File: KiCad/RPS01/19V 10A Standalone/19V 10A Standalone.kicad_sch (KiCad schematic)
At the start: 33 parts, among them U2 LTC3780EUH-TRPBF

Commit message: 19V 10A Standalone PCB
Updated the standalone 19V 10A PCB. Just needs the connectors.
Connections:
- net BOOST2: no longer Cb(SW2)1.1, D1(2)_19V1.1, L1_19V1.1, QA(1)_19V_2.1, QA(1)_19V_2.2, QA(1)_19V_2.3, QB(2)_19V_1.5, QB(2)_19V_1.6, QB(2)_19V_1.7, QB(2)_19V_1.8, U2.17 (SW2)
- new net SW2: Cb(SW2)1.1, D1(2)_19V1.1, L1_19V1.1, QA(1)_19V_2.1, QA(1)_19V_2.2, QA(1)_19V_2.3, QB(2)_19V_1.5, QB(2)_19V_1.6, QB(2)_19V_1.7, QB(2)_19V_1.8, U2.17 (SW2)
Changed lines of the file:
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@@
 (kicad_sch (version 20230121) (generator eeschema)
   (paper "A4")
-  (junction (at 209.806 79.375) (diameter 0) (color 0 0 0 0)
-  )
   (junction (at 53.34 92.075) (diameter 0) (color 0 0 0 0)
   )
@@
   )
   (junction (at 58.42 99.695) (diameter 0) (color 0 0 0 0)
-  )
-  (junction (at 209.806 132.08) (diameter 0) (color 0 0 0 0)
   )
   (junction (at 231.14 31.115) (diameter 0) (color 0 0 0 0)
@@
     (stroke (width 0) (type default))
   )
+  (wire (pts (xy 217.17 79.375) (xy 217.17 163.83))
+    (stroke (width 0) (type default))
+  )
   (wire (pts (xy 175.8696 114.2746) (xy 185.42 114.3))
     (stroke (width 0) (type default))
@@
     (stroke (width 0) (type default))
   )
+  (wire (pts (xy 184.15 154.94) (xy 184.15 163.83))
+    (stroke (width 0) (type default))
+  )
   (wire (pts (xy 184.15 154.94) (xy 184.15 153.035))
     (stroke (width 0) (type default))
@@
     (stroke (width 0) (type default))
   )
-  (wire (pts (xy 234.6942 138.4026) (xy 234.6942 163.1421))
-    (stroke (width 0) (type default))
-  )
   (wire (pts (xy 53.34 88.773) (xy 53.34 92.075))
     (stroke (width 0) (type default))
@@
     (stroke (width 0) (type default))
   )
-  (wire (pts (xy 209.806 132.08) (xy 213.36 132.08))
-    (stroke (width 0) (type default))
-  )
   (wire (pts (xy 48.26 132.715) (xy 53.975 132.715))
     (stroke (width 0) (type default))
@@
     (stroke (width 0) (type default))
   )
-  (wire (pts (xy 184.15 163.1421) (xy 184.15 154.94))
-    (stroke (width 0) (type default))
-  )
   (wire (pts (xy 233.68 56.515) (xy 233.68 33.655))
     (stroke (width 0) (type default))
@@
     (stroke (width 0) (type default))
   )
-  (wire (pts (xy 184.15 163.1421) (xy 234.6942 163.1421))
-    (stroke (width 0) (type default))
-  )
   (wire (pts (xy 175.26 120.65) (xy 175.26 137.16))
     (stroke (width 0) (type default))
   )
-  (wire (pts (xy 209.806 79.375) (xy 209.806 132.08))
-    (stroke (width 0) (type default))
-  )
   (wire (pts (xy 132.08 28.575) (xy 132.08 31.115))
     (stroke (width 0) (type default))
@@
     (stroke (width 0) (type default))
   )
-  (wire (pts (xy 161.29 79.375) (xy 209.806 79.375))
-    (stroke (width 0) (type default))
-  )
   (wire (pts (xy 180.34 31.115) (xy 180.34 33.655))
     (stroke (width 0) (type default))
@@
     (stroke (width 0) (type default))
   )
-  (wire (pts (xy 234.6942 138.4026) (xy 213.36 138.4026))
-    (stroke (width 0) (type default))
-  )
   (wire (pts (xy 54.3814 71.2724) (xy 54.3814 88.773))
     (stroke (width 0) (type default))
@@
     (stroke (width 0) (type default))
   )
+  (wire (pts (xy 217.17 163.83) (xy 184.15 163.83))
+    (stroke (width 0) (type default))
+  )
   (wire (pts (xy 53.34 107.315) (xy 58.42 107.315))
     (stroke (width 0) (type default))
   )
-  (wire (pts (xy 209.806 48.9753) (xy 209.806 79.375))
+  (wire (pts (xy 209.806 48.9753) (xy 209.806 132.08))
     (stroke (width 0) (type default))
   )
@@
     (stroke (width 0) (type default))
   )
+  (wire (pts (xy 161.29 79.375) (xy 217.17 79.375))
+    (stroke (width 0) (type default))
+  )
   (wire (pts (xy 102.87 149.86) (xy 102.87 151.13))
     (stroke (width 0) (type default))
@@
     (stroke (width 0) (type default))
   )
-  (wire (pts (xy 213.36 132.08) (xy 213.36 138.4026))
-    (stroke (width 0) (type default))
-  )

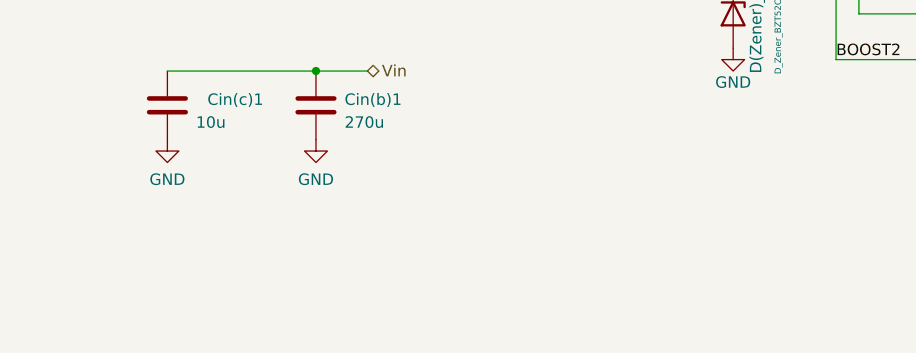
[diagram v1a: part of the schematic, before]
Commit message: 19V 10A Standalone PCB
Final design of the Boost converter should be finished, double check if possible please!
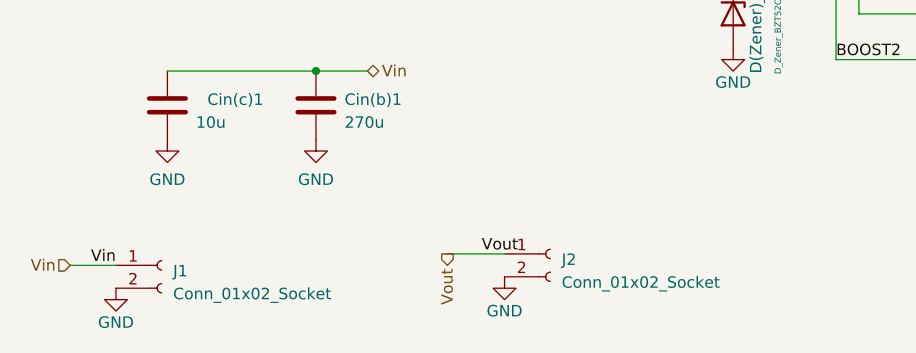
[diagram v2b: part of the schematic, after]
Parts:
- added J1: Conn_01x02_Socket, Mechatronic Footprints:AMASS_XT60-M_1x02_P7.20mm_Vertical, symbol Connector:Conn_01x02_Socket
- added J2: Conn_01x02_Socket, Mechatronic Footprints:AMASS_XT60-F_1x02_P7.20mm_Vertical, symbol Connector:Conn_01x02_Socket
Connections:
- net GND: now also J1.2 (Pin_2), J2.2 (Pin_2)
- net Vin: now also J1.1 (Pin_1)
- net Vout: now also J2.1 (Pin_1)
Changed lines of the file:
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@@
+    (stroke (width 0) (type default))
+  )
+  (wire (pts (xy 71.12 181.61) (xy 77.47 181.61))
     (stroke (width 0) (type default))
   )
@@
   )
   (wire (pts (xy 78.74 99.695) (xy 90.17 99.695))
+    (stroke (width 0) (type default))
+  )
+  (wire (pts (xy 29.21 182.88) (xy 34.29 182.88))
     (stroke (width 0) (type default))
   )
@@
     (effects (font (size 1.27 1.27)) (justify left bottom))
   )
+  (label "Vin" (at 34.29 182.88 180) (fields_autoplaced)
+    (effects (font (size 1.27 1.27)) (justify right bottom))
+  )
   (label "STBYMD" (at 113.2332 132.08 0) (fields_autoplaced)
     (effects (font (size 1.27 1.27)) (justify left bottom))
@@
     (effects (font (size 1.27 1.27)) (justify left bottom))
   )
+  (label "Vout" (at 74.93 181.61 0) (fields_autoplaced)
+    (effects (font (size 1.27 1.27)) (justify left bottom))
+  )
   (label "GND" (at 115.7478 124.46 0) (fields_autoplaced)
     (effects (font (size 1 1)) (justify left bottom))
   )
+  (hierarchical_label "Vin" (shape input) (at 29.21 182.88 180) (fields_autoplaced)
+    (effects (font (size 1.27 1.27)) (justify right))
+  )
   (hierarchical_label "Vin" (shape bidirectional) (at 62.23 161.29 0) (fields_autoplaced)
     (effects (font (size 1.27 1.27)) (justify left))
@@
     (effects (font (size 1.27 1.27)) (justify left))
   )
+  (hierarchical_label "Vout" (shape output) (at 71.12 181.61 270) (fields_autoplaced)
+    (effects (font (size 1.27 1.27)) (justify right))
+  )
   (hierarchical_label "Vin" (shape input) (at 182.88 41.275 0) (fields_autoplaced)
     (effects (font (size 1.27 1.27)) (justify left))
@@
     (effects (font (size 1.27 1.27)) (justify left))
   )
+  (symbol (lib_id "Connector:Conn_01x02_Socket") (at 39.37 182.88 0) (unit 1)
+    (in_bom yes) (on_board yes) (dnp no) (fields_autoplaced)
+    (property "Reference" "J1" (at 40.64 183.515 0)
+      (effects (font (size 1.27 1.27)) (justify left))
+    )
+    (property "Value" "Conn_01x02_Socket" (at 40.64 186.055 0)
+      (effects (font (size 1.27 1.27)) (justify left))
+    )
+    (property "Footprint" "Mechatronic Footprints:AMASS_XT60-M_1x02_P7.20mm_Vertical" (at 39.37 182.88 0)
+      (effects (font (size 1.27 1.27)) hide)
+    )
+    (property "Datasheet" "~" (at 39.37 182.88 0)
+      (effects (font (size 1.27 1.27)) hide)
+    )
+    (pin "1")
+    (pin "2")
+    (instances
+      (project "19V 10A Standalone"
+        (path "/c6cb6fed-0376-4b68-94de-cc093c2b764e"
+          (reference "J1") (unit 1)
+        )
+      )
+    )
+  )
   (symbol (lib_id "Device:R") (at 72.39 136.525 0) (unit 1)
     (in_bom yes) (on_board yes) (dnp no) (fields_autoplaced)
@@
         (path "/c6cb6fed-0376-4b68-94de-cc093c2b764e"
           (reference "#PWR02") (unit 1)
+        )
+      )
+    )
+  )
+  (symbol (lib_id "power:GND") (at 34.29 185.42 0) (unit 1)
+    (in_bom yes) (on_board yes) (dnp no) (fields_autoplaced)
+    (property "Reference" "#PWR0109" (at 34.29 191.77 0)
+      (effects (font (size 1.27 1.27)) hide)
+    )
+    (property "Value" "GND" (at 34.29 189.23 0)
+      (effects (font (size 1.27 1.27)))
+    )
+    (property "Footprint" "" (at 34.29 185.42 0)
+      (effects (font (size 1.27 1.27)) hide)
+    )
+    (property "Datasheet" "" (at 34.29 185.42 0)
+      (effects (font (size 1.27 1.27)) hide)
+    )
+    (pin "1")
+    (instances
+      (project "rps01"
+        (path "/14930f15-c0a0-4b55-93e6-b112548415f6/c502224c-4356-4e96-bcfe-3f158512eab2"
+          (reference "#PWR0109") (unit 1)
+        )
+      )
+      (project "19V 10A Standalone"
+        (path "/c6cb6fed-0376-4b68-94de-cc093c2b764e"
+          (reference "#PWR021") (unit 1)
         )
       )
@@
     )
   )
+  (symbol (lib_id "Connector:Conn_01x02_Socket") (at 82.55 181.61 0) (unit 1)
+    (in_bom yes) (on_board yes) (dnp no) (fields_autoplaced)
+    (property "Reference" "J2" (at 83.82 182.245 0)
+      (effects (font (size 1.27 1.27)) (justify left))
+    )
+    (property "Value" "Conn_01x02_Socket" (at 83.82 184.785 0)
+      (effects (font (size 1.27 1.27)) (justify left))
+    )
+    (property "Footprint" "Mechatronic Footprints:AMASS_XT60-F_1x02_P7.20mm_Vertical" (at 82.55 181.61 0)
+      (effects (font (size 1.27 1.27)) hide)
+    )
+    (property "Datasheet" "~" (at 82.55 181.61 0)
+      (effects (font (size 1.27 1.27)) hide)
+    )
+    (pin "1")
+    (pin "2")
+    (instances
+      (project "19V 10A Standalone"
+        (path "/c6cb6fed-0376-4b68-94de-cc093c2b764e"
+          (reference "J2") (unit 1)
+        )
+      )
+    )
+  )
   (symbol (lib_id "Device:C") (at 190.5 153.035 270) (unit 1)
     (in_bom yes) (on_board yes) (dnp no)
@@
         )
       )
+    )
+  )
+  (symbol (lib_id "power:GND") (at 77.47 184.15 0) (unit 1)
+    (in_bom yes) (on_board yes) (dnp no) (fields_autoplaced)
+    (property "Reference" "#PWR0109" (at 77.47 190.5 0)
+      (effects (font (size 1.27 1.27)) hide)
+    )
+    (property "Value" "GND" (at 77.47 187.96 0)
+      (effects (font (size 1.27 1.27)))
+    )
+    (property "Footprint" "" (at 77.47 184.15 0)
+      (effects (font (size 1.27 1.27)) hide)
+    )
+    (property "Datasheet" "" (at 77.47 184.15 0)
+      (effects (font (size 1.27 1.27)) hide)
+    )
+    (pin "1")
+    (instances
+      (project "rps01"
+        (path "/14930f15-c0a0-4b55-93e6-b112548415f6/c502224c-4356-4e96-bcfe-3f158512eab2"
+          (reference "#PWR0109") (unit 1)
+        )
+      )
+      (project "19V 10A Standalone"
+        (path "/c6cb6fed-0376-4b68-94de-cc093c2b764e"
+          (reference "#PWR020") (unit 1)
+        )
+      )
